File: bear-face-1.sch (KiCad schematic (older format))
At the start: 177 parts, among them J1 Conn_01x04, SW1 SW_Push, U1 Elite-C

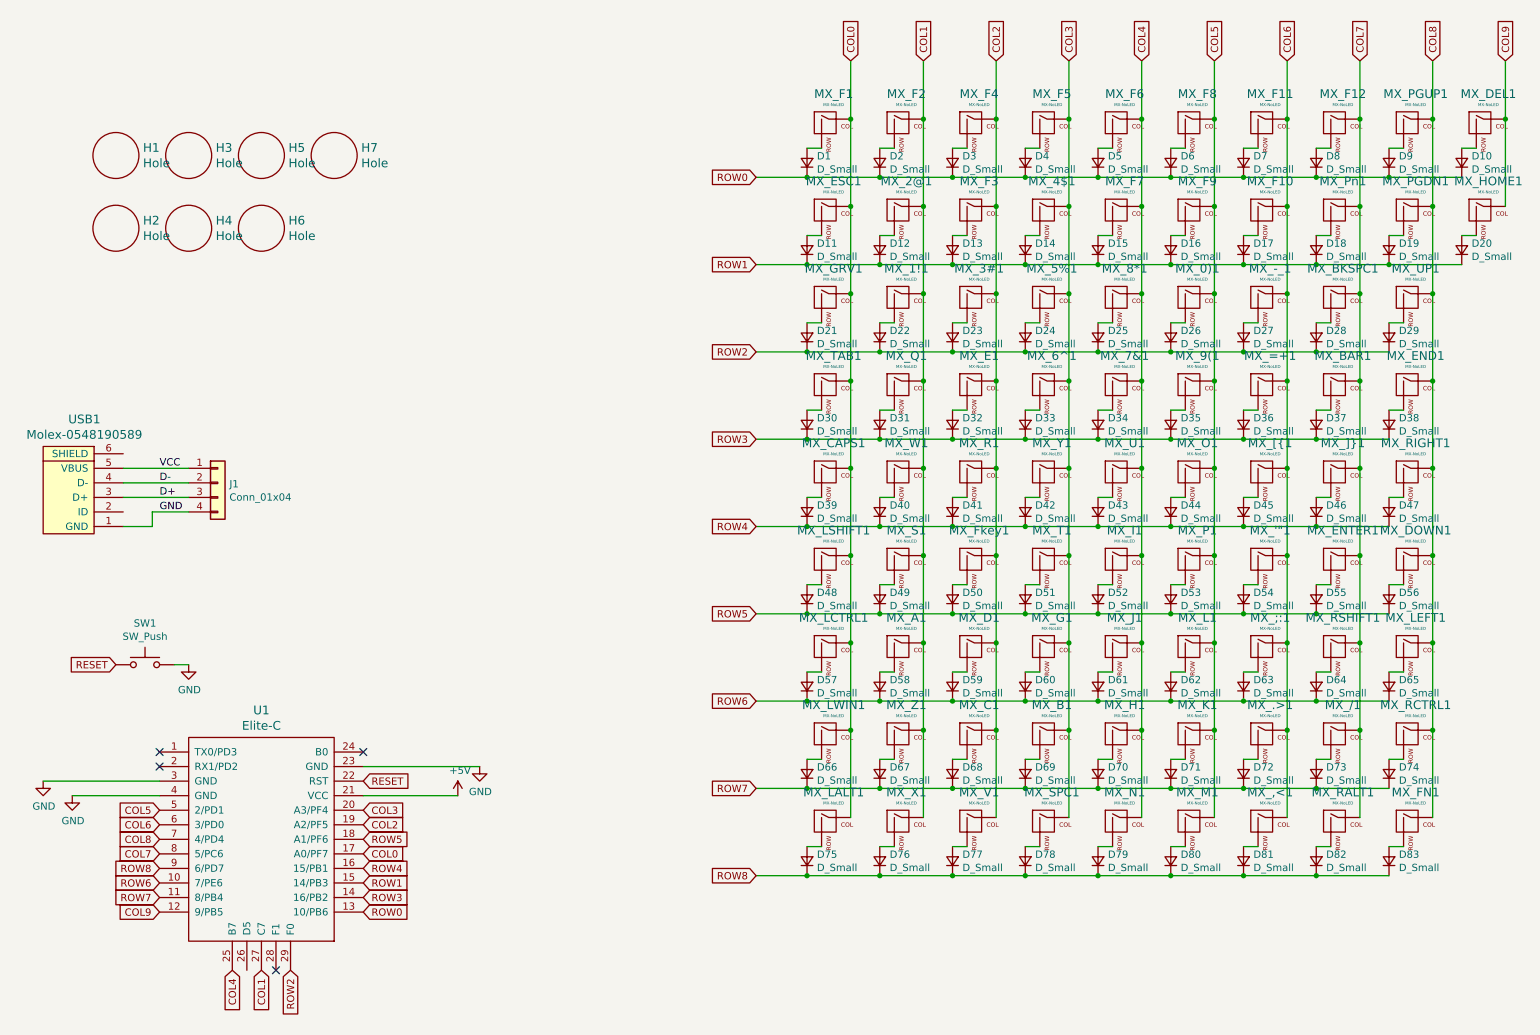
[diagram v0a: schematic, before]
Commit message: Massive update
Changed names to Bear Face 1, moved Elite-C to under the spacebar & updated tracks as necessary. Need to check mounting hole positions, but other than that almost ready for gerbers
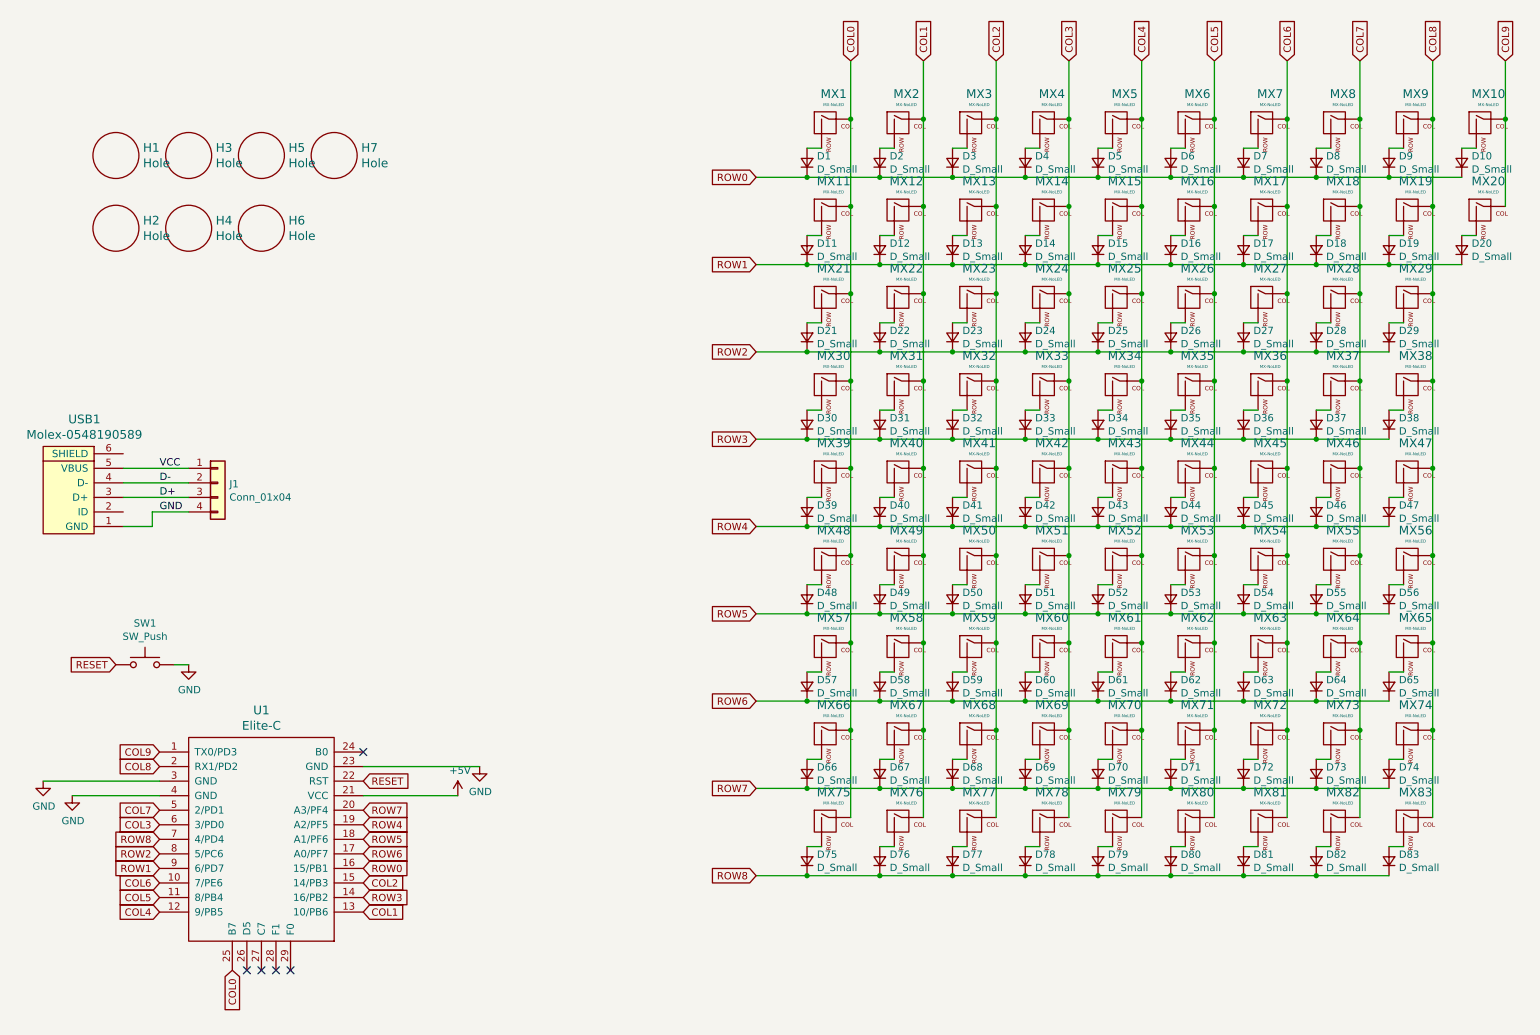
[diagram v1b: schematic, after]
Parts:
- MX78: renamed from MX_SPC1; footprint MX_Only:MXOnly-6.25U -> MX_Only:MXOnly-6.25U-NoLED
- renumbered MX_F1 to MX1, MX_DEL1 to MX10, MX_ESC1 to MX11, MX_2@1 to MX12, MX_F3 to MX13, MX_4$1 to MX14, MX_F7 to MX15, MX_F9 to MX16, MX_F10 to MX17, MX_Pn1 to MX18, MX_PGDN1 to MX19, MX_F2 to MX2, MX_HOME1 to MX20, MX_GRV1 to MX21, MX_1!1 to MX22, MX_3#1 to MX23, MX_5%1 to MX24, MX_8*1 to MX25, MX_0)1 to MX26, MX_-_1 to MX27, MX_BKSPC1 to MX28, MX_UP1 to MX29, MX_F4 to MX3, MX_TAB1 to MX30, MX_Q1 to MX31, MX_E1 to MX32, MX_6^1 to MX33, MX_7&1 to MX34, MX_9(1 to MX35, MX_=+1 to MX36, MX_BAR1 to MX37, MX_END1 to MX38, MX_CAPS1 to MX39, MX_F5 to MX4, MX_W1 to MX40, MX_R1 to MX41, MX_Y1 to MX42, MX_U1 to MX43, MX_O1 to MX44, MX_[{1 to MX45, MX_]}1 to MX46, MX_RIGHT1 to MX47, MX_LSHIFT1 to MX48, MX_S1 to MX49, MX_F6 to MX5, MX_Fkey1 to MX50, MX_T1 to MX51, MX_I1 to MX52, MX_P1 to MX53, MX_'"1 to MX54, MX_ENTER1 to MX55, MX_DOWN1 to MX56, MX_LCTRL1 to MX57, MX_A1 to MX58, MX_D1 to MX59, MX_F8 to MX6, MX_G1 to MX60, MX_J1 to MX61, MX_L1 to MX62, MX_;:1 to MX63, MX_RSHIFT1 to MX64, MX_LEFT1 to MX65, MX_LWIN1 to MX66, MX_Z1 to MX67, MX_C1 to MX68, MX_B1 to MX69, MX_F11 to MX7, MX_H1 to MX70, MX_K1 to MX71, MX_.>1 to MX72, MX_/1 to MX73, MX_RCTRL1 to MX74, MX_LALT1 to MX75, MX_X1 to MX76, MX_V1 to MX77, MX_N1 to MX79, MX_F12 to MX8, MX_M1 to MX80, MX_,<1 to MX81, MX_RALT1 to MX82, MX_FN1 to MX83, MX_PGUP1 to MX9
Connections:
- net COL0: now also U1.25 (B7); no longer U1.17 (A0/PF7)
- net COL1: now also U1.13 (10/PB6); no longer U1.27 (C7)
- net COL2: now also U1.15 (14/PB3); no longer U1.19 (A2/PF5)
- net COL3: now also U1.6 (3/PD0); no longer U1.20 (A3/PF4)
- net COL4: now also U1.12 (9/PB5); no longer U1.25 (B7)
- net COL5: now also U1.11 (8/PB4); no longer U1.5 (2/PD1)
- net COL6: now also U1.10 (7/PE6); no longer U1.6 (3/PD0)
- net COL7: now also U1.5 (2/PD1); no longer U1.8 (5/PC6)
- net COL8: now also U1.2 (RX1/PD2); no longer U1.7 (4/PD4)
- net COL9: now also U1.1 (TX0/PD3); no longer U1.12 (9/PB5)
- net ROW0: now also U1.16 (15/PB1); no longer U1.13 (10/PB6)
- net ROW1: now also U1.9 (6/PD7); no longer U1.15 (14/PB3)
- net ROW2: now also U1.8 (5/PC6); no longer U1.29 (F0)
- net ROW4: now also U1.19 (A2/PF5); no longer U1.16 (15/PB1)
- net ROW6: now also U1.17 (A0/PF7); no longer U1.10 (7/PE6)
- net ROW7: now also U1.20 (A3/PF4); no longer U1.11 (8/PB4)
- net ROW8: now also U1.7 (4/PD4); no longer U1.9 (6/PD7)
- no-connect marks 4 -> 5
